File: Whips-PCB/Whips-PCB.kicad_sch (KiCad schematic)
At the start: 22 parts, among them J1 Micro_SD_Card, SW2 SW_DIP_x06, U1 Teensy4.0, U2 MAX485E, U3 SN74AHCT125, U4 TSR_1-2450, U5 MAX98357AEWL_T

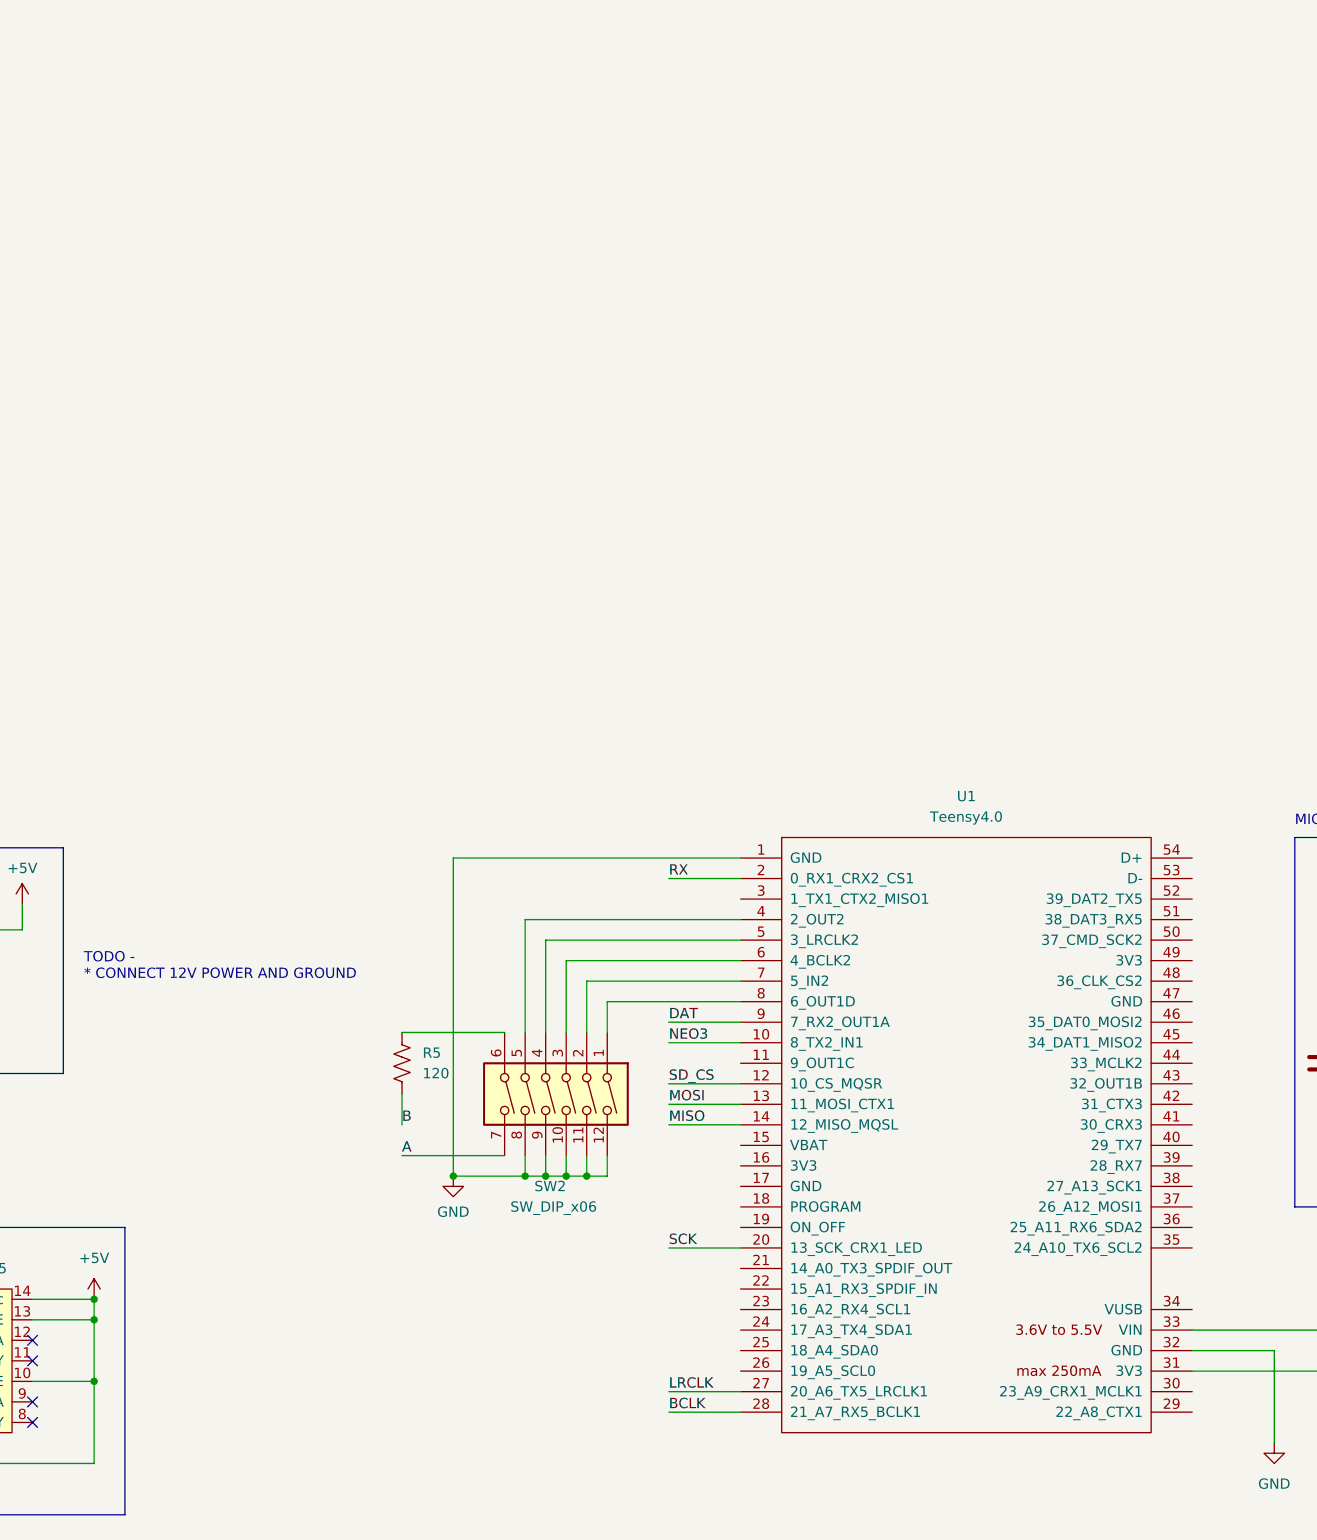
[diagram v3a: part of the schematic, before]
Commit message: pots for brightness (not implemented), volume
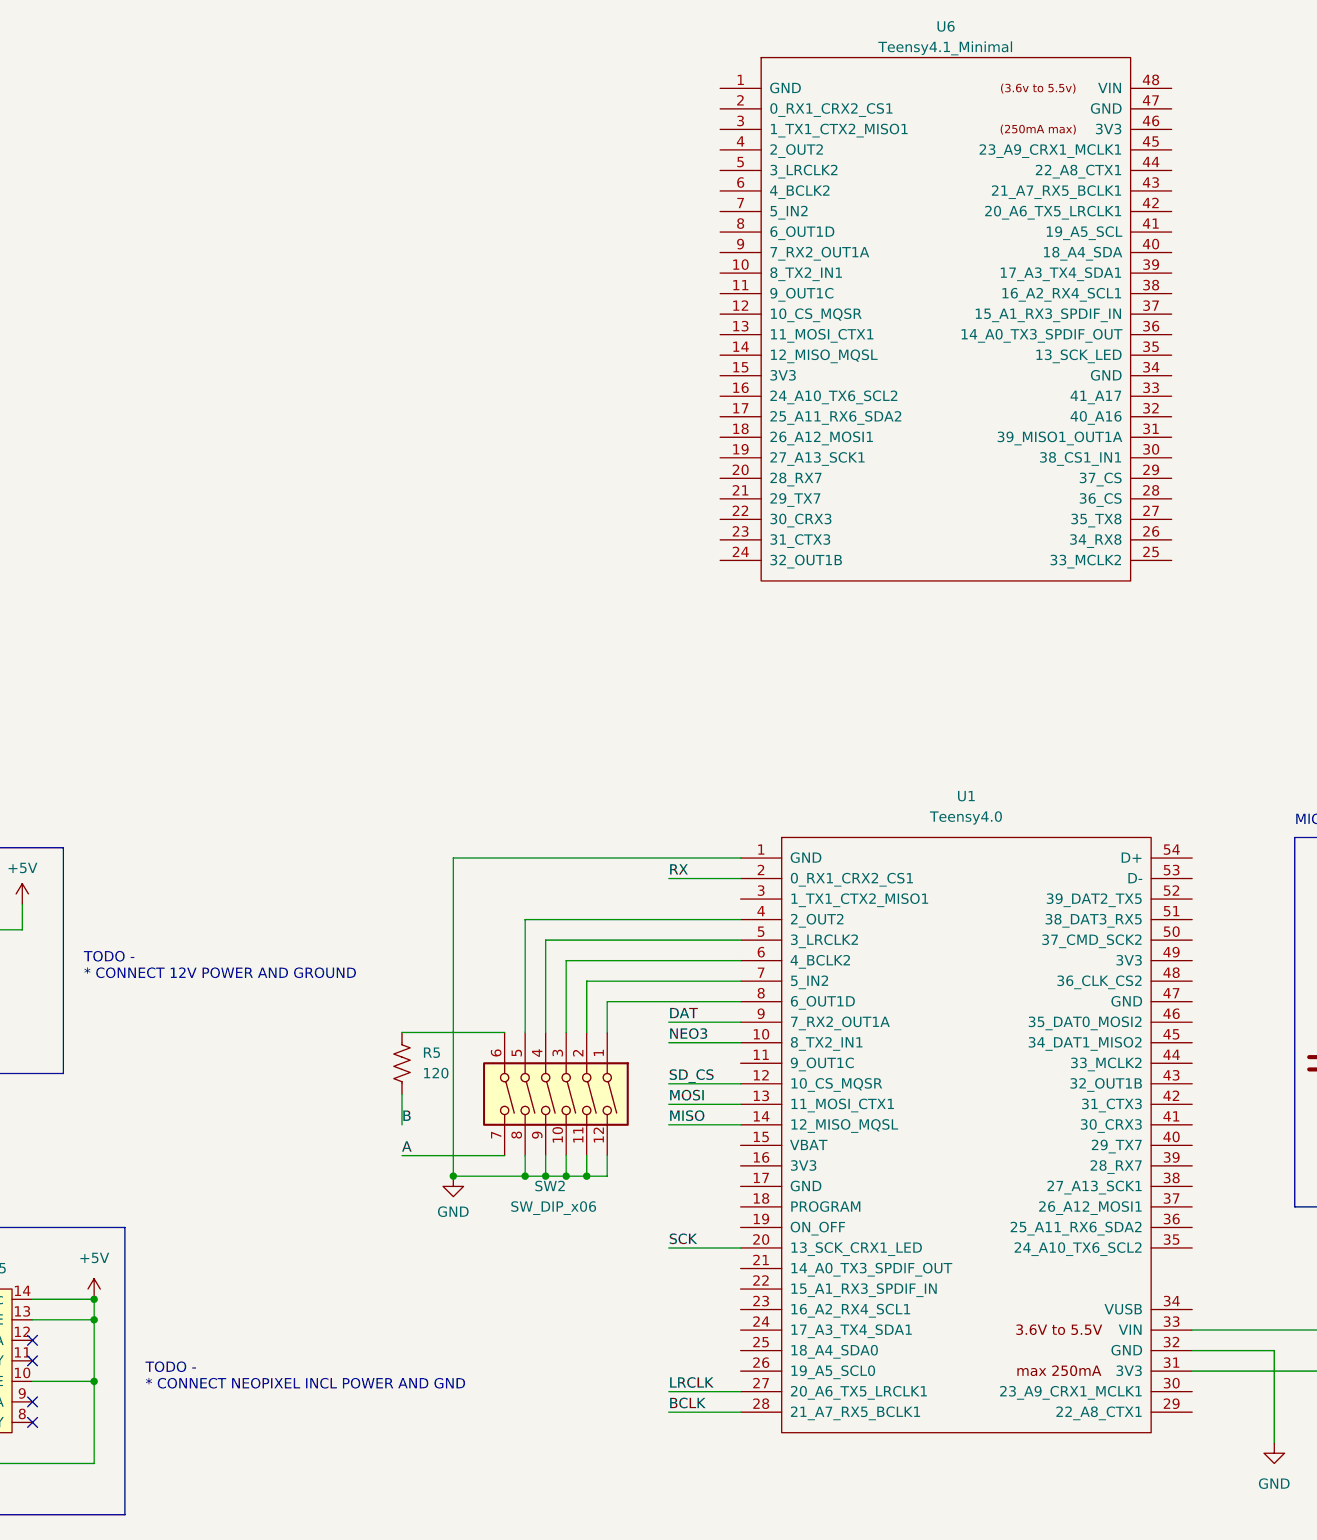
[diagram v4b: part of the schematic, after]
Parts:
- added U6: Teensy4.1_Minimal, symbol Joels KiCad Symbol Library:Teensy4.1_Minimal
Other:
- note added: "TODO - * CONNECT NEOPIXEL INCL POWER AND GND"
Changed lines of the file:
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@@
+    (effects (font (size 1.27 1.27)) (justify left bottom))
+  )
+  (text "TODO - \n* CONNECT NEOPIXEL INCL POWER AND GND" (at 62.23 92.71 0)
     (effects (font (size 1.27 1.27)) (justify left bottom))
   )
@@
         )
       )
+    )
+  )
+  (symbol (lib_id "Joels KiCad Symbol Library:Teensy4.1_Minimal") (at 161.29 -13.97 0) (unit 1)
+    (in_bom yes) (on_board yes) (dnp no) (fields_autoplaced)
+    (property "Reference" "U6" (at 161.29 -76.2 0)
+      (effects (font (size 1.27 1.27)))
+    )
+    (property "Value" "Teensy4.1_Minimal" (at 161.29 -73.66 0)
+      (effects (font (size 1.27 1.27)))
+    )
+    (property "Footprint" "" (at 151.13 -24.13 0)
+      (effects (font (size 1.27 1.27)) hide)
+    )
+    (property "Datasheet" "" (at 151.13 -24.13 0)
+      (effects (font (size 1.27 1.27)) hide)
+    )
+    (pin "10")
+    (pin "11")
+    (pin "12")
+    (pin "13")
+    (pin "14")
+    (pin "15")
+    (pin "16")
+    (pin "17")
+    (pin "18")
+    (pin "19")
+    (pin "20")
+    (pin "21")
+    (pin "22")
+    (pin "23")
+    (pin "24")
+    (pin "25")
+    (pin "26")
+    (pin "27")
+    (pin "28")
+    (pin "29")
+    (pin "30")
+    (pin "31")
+    (pin "32")
+    (pin "33")
+    (pin "35")
+    (pin "36")
+    (pin "37")
+    (pin "38")
+    (pin "39")
+    (pin "40")
+    (pin "41")
+    (pin "42")
+    (pin "43")
+    (pin "44")
+    (pin "45")
+    (pin "46")
+    (pin "47")
+    (pin "48")
+    (pin "5")
+    (pin "6")
+    (pin "7")
+    (pin "8")
+    (pin "9")
+    (pin "1")
+    (pin "2")
+    (pin "3")
+    (pin "34")
+    (pin "4")
+    (instances
+      (project "Whips-PCB"
+        (path "/f51f4695-2f3c-4442-ab83-4885bbbb2720"
+          (reference "U6") (unit 1)
+        )
+      )

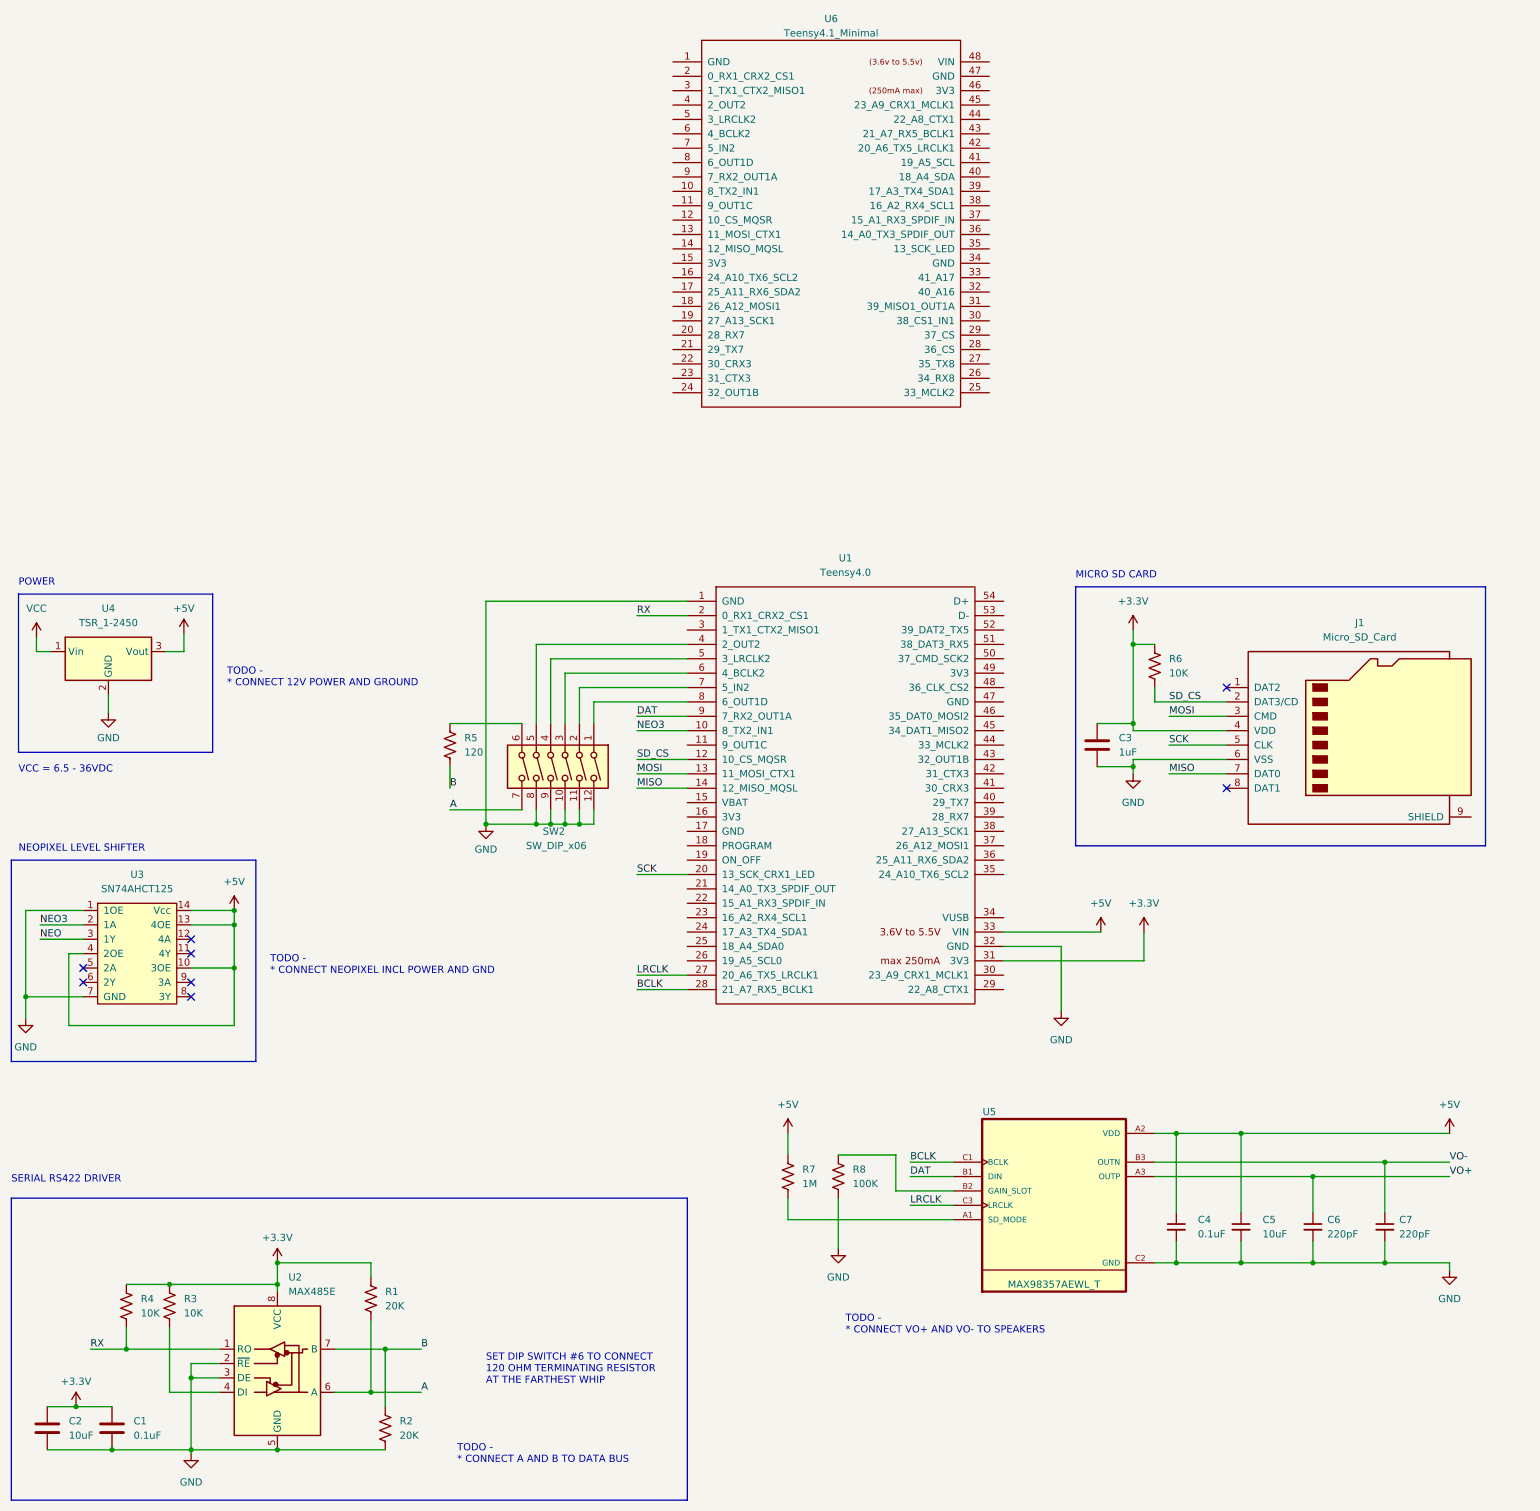
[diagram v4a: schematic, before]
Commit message: teensy 4.0->4.1
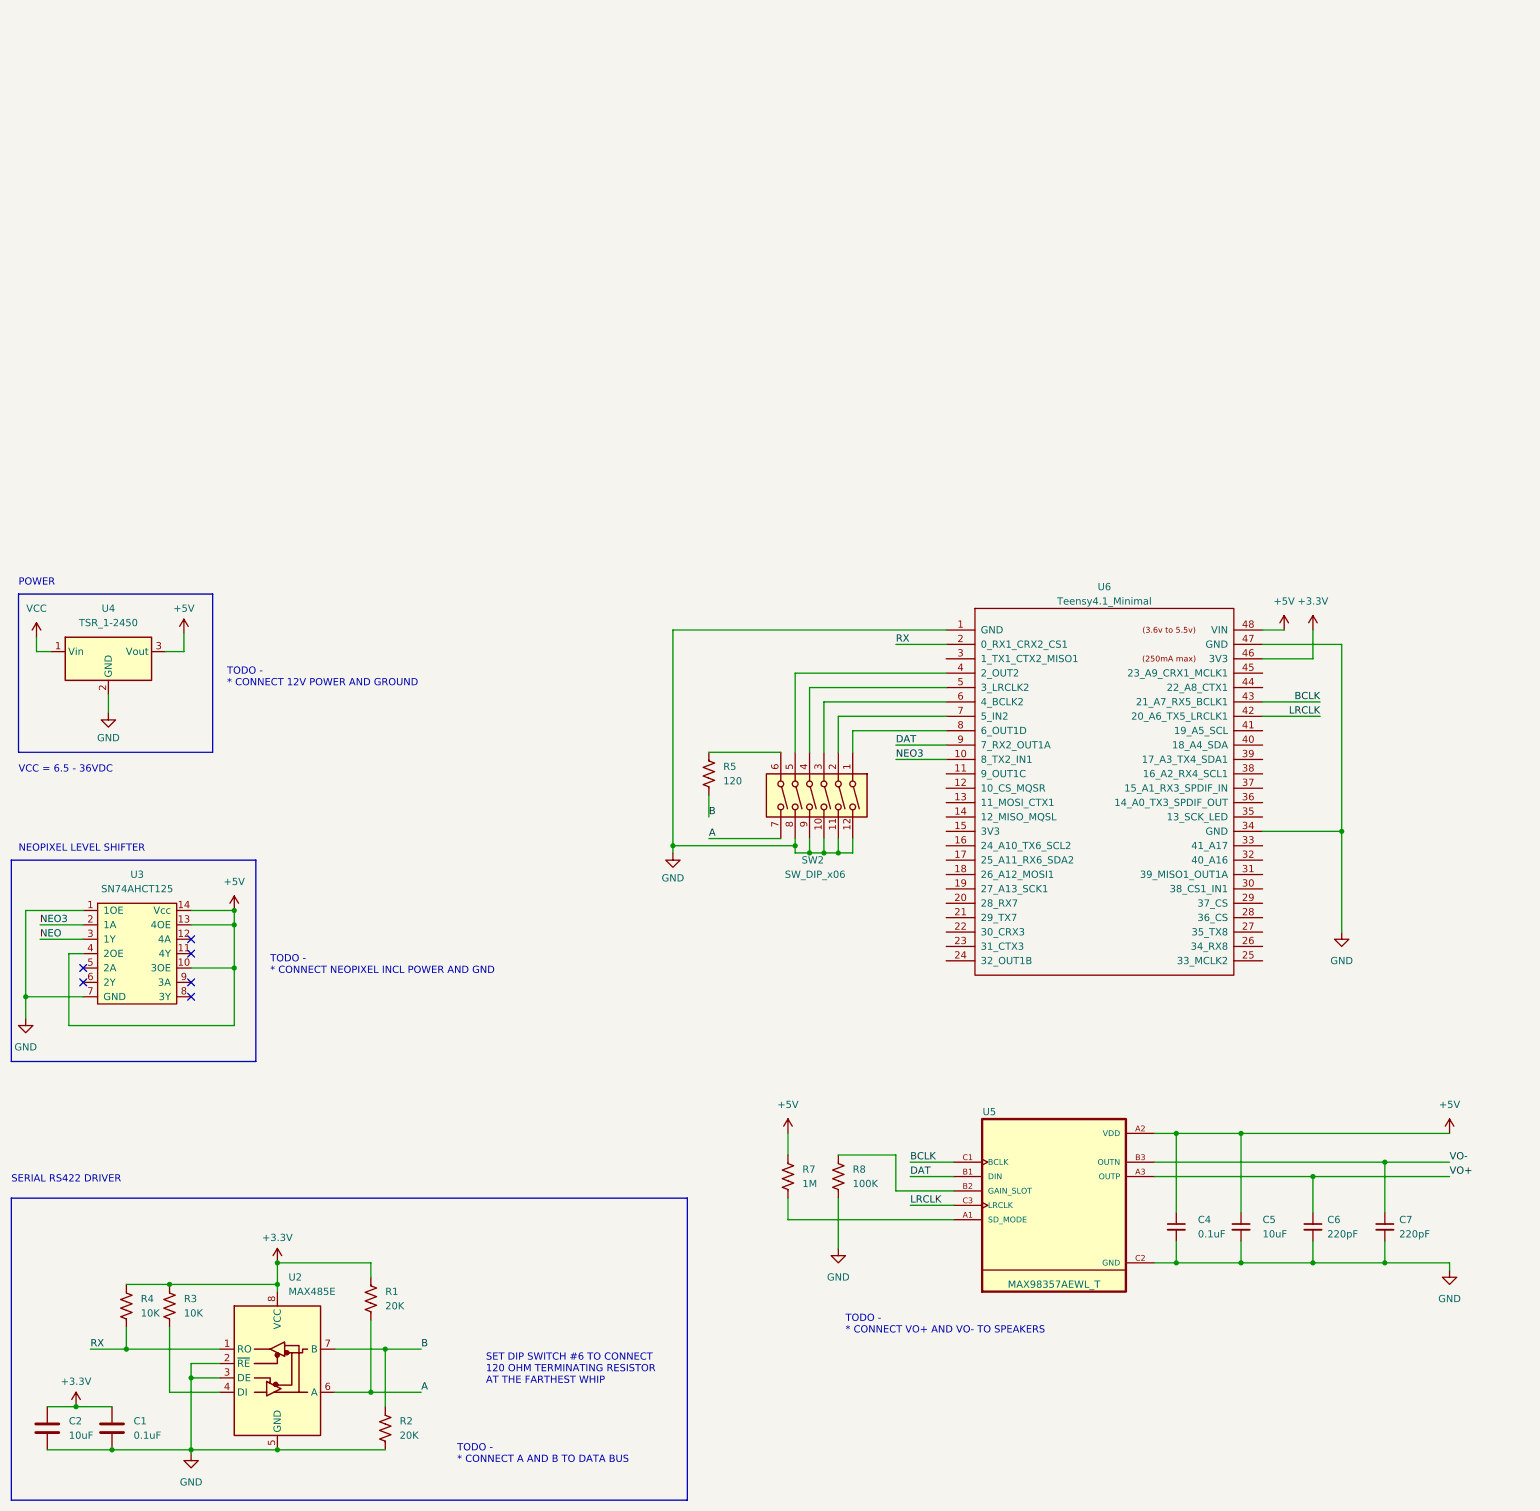
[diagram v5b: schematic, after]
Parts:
- removed C3: 1uF, symbol Device:C
- removed J1: Micro_SD_Card, symbol Connector:Micro_SD_Card
- removed R6: 10K, symbol Device:R_US
- removed U1: Teensy4.0, symbol teensy:Teensy4.0
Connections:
- net +3.3V: now also U6.46 (3V3)
- net +5V: now also U6.48 (VIN)
- net BCLK: now also U6.43 (21_A7_RX5_BCLK1)
- net DAT: now also U6.9 (7_RX2_OUT1A)
- net GND: now also U6.1 (GND), U6.34 (GND), U6.47 (GND)
- net LRCLK: now also U6.42 (20_A6_TX5_LRCLK1)
- net NEO3: now also U6.10 (8_TX2_IN1)
- net RX: now also U6.2 (0_RX1_CRX2_CS1)
- net at U6.4 (2_OUT2): now also SW2.5
- net at U6.5 (3_LRCLK2): now also SW2.4
- net at U6.6 (4_BCLK2): now also SW2.3
- net at U6.7 (5_IN2): now also SW2.2
- net at U6.8 (6_OUT1D): now also SW2.1
- no-connect marks 8 -> 6
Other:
- note removed: "MICRO SD CARD"
- moved on the sheet: R5, SW2, U6

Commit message: starting to find part numbers and footprints
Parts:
- added J1: 12 VDC, symbol Connector_Generic:Conn_01x02
- added J2: RS422 BUS, symbol Connector_Generic:Conn_01x02
- added J3: SPEAKER 4OHM, symbol Connector_Generic:Conn_01x02
- added J4: TO WHIP, symbol Connector_Generic:Conn_01x03
- C1, C4: footprint (none) -> Capacitor_SMD:C_0201_0603Metric; LCSC (none) -> C76934
- C2, C5: footprint (none) -> Capacitor_SMD:C_0603_1608Metric; LCSC (none) -> C1691
- C6, C7: footprint (none) -> Capacitor_SMD:C_0402_1005Metric; LCSC (none) -> C1530
- R1, R2: footprint (none) -> Resistor_SMD:R_0603_1608Metric; LCSC (none) -> C4184
- R3, R4: footprint (none) -> Resistor_SMD:R_0603_1608Metric; LCSC (none) -> C25804
- R5: footprint (none) -> Resistor_SMD:R_0402_1005Metric; LCSC (none) -> C25079
- R7: footprint (none) -> Resistor_SMD:R_0402_1005Metric; LCSC (none) -> C26083
- R8: footprint (none) -> Resistor_SMD:R_0805_2012Metric; LCSC (none) -> C149504
- SW2: LCSC (none) -> C5160843
- U2: value MAX485E -> MAX485ESA+T; footprint (none) -> Package_SO:SOIC-8-1EP_3.9x4.9mm_P1.27mm_EP2.29x3mm; LCSC (none) -> C19738
- U3: value SN74AHCT125 -> SN74AHCT125DR; footprint (none) -> Package_SO:SOIC-14_3.9x8.7mm_P1.27mm; LCSC (none) -> C155176
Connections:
- net A: now also J2.2 (Pin_2)
- net B: now also J2.1 (Pin_1)
- net GND: now also J1.1 (Pin_1), J4.3 (Pin_3)
- net NEO: now also J4.2 (Pin_2)
- net VO+: now also J3.2 (Pin_2)
- net VO-: now also J3.1 (Pin_1)
- net VCC renamed 12VDC
- net 12VDC: now also J1.2 (Pin_2), J4.1 (Pin_1)
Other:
- note removed: "TODO - * CONNECT 12V POWER AND GROUND"
- note removed: "TODO - * CONNECT A AND B TO DATA BUS"
- note removed: "TODO - * CONNECT NEOPIXEL INCL POWER AND GND"
- note removed: "TODO - * CONNECT VO+ AND VO- TO SPEAKERS"
- note removed: "VCC = 6.5 - 36VDC"
- moved on the sheet: C4, C5, C6, C7, R7, R8, U3, U4, U5
